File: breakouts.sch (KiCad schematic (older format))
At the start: 27 parts, among them P10 CONN_8, P11 CONN_5, P12 CONN_5, P13 CONN_6, P14 CONN_8, P15 CONN_5X2, P16 CONN_16, P17 CONN_16, P18 POWER, P19 PCM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

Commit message: A bunch of footprint arranging
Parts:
- P25: renamed from P?; footprint (none) -> replacement_kinesis_controller:Pin_Header_Staggered_Straight_1x02
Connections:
- net RST renamed RESET
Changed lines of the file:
@@
 PD1
 $Comp
-L GND #PWR35
+L GND #PWR034
 U 1 1 54E556E0
 P 2450 6050
-F 0 "#PWR35" H 2450 6050 30  0001 C CNN
+F 0 "#PWR034" H 2450 6050 30  0001 C CNN
 F 1 "GND" H 2450 5980 30  0001 C CNN
 F 2 "" H 2450 6050 60  0000 C CNN
@@
 $EndComp
 $Comp
-L GND #PWR37
+L GND #PWR035
 U 1 1 54E556E6
 P 4750 6050
-F 0 "#PWR37" H 4750 6050 30  0001 C CNN
+F 0 "#PWR035" H 4750 6050 30  0001 C CNN
 F 1 "GND" H 4750 5980 30  0001 C CNN
 F 2 "" H 4750 6050 60  0000 C CNN
@@
 $EndComp
 $Comp
-L VCC #PWR34
+L VCC #PWR036
 U 1 1 54E556EC
 P 2450 5800
-F 0 "#PWR34" H 2450 5900 30  0001 C CNN
+F 0 "#PWR036" H 2450 5900 30  0001 C CNN
 F 1 "VCC" H 2450 5900 30  0000 C CNN
 F 2 "" H 2450 5800 60  0000 C CNN
@@
 $EndComp
 $Comp
-L VCC #PWR36
+L VCC #PWR037
 U 1 1 54E556F2
 P 4750 5800
-F 0 "#PWR36" H 4750 5900 30  0001 C CNN
+F 0 "#PWR037" H 4750 5900 30  0001 C CNN
 F 1 "VCC" H 4750 5900 30  0000 C CNN
 F 2 "" H 4750 5800 60  0000 C CNN
@@
 	4750 5900 4750 5800
 $Comp
-L +5V #PWR39
+L +5V #PWR038
 U 1 1 54E569F6
 P 6250 2900
-F 0 "#PWR39" H 6250 2990 20  0001 C CNN
+F 0 "#PWR038" H 6250 2990 20  0001 C CNN
 F 1 "+5V" H 6250 2990 30  0000 C CNN
 F 2 "" H 6250 2900 60  0000 C CNN
@@
 PB4
 $Comp
-L GND #PWR38
+L GND #PWR039
 U 1 1 54E56A09
 P 5700 4500
-F 0 "#PWR38" H 5700 4500 30  0001 C CNN
+F 0 "#PWR039" H 5700 4500 30  0001 C CNN
 F 1 "GND" H 5700 4430 30  0001 C CNN
 F 2 "" H 5700 4500 60  0000 C CNN
@@
 PE6
 $Comp
-L +3.3V #PWR40
+L +3.3V #PWR040
 U 1 1 54E56A23
 P 7450 2900
-F 0 "#PWR40" H 7450 2860 30  0001 C CNN
+F 0 "#PWR040" H 7450 2860 30  0001 C CNN
 F 1 "+3.3V" H 7450 3010 30  0000 C CNN
 F 2 "" H 7450 2900 60  0000 C CNN
@@
 $EndComp
 Text GLabel 6100 4500 0    60   Input ~ 0
-RST
+RESET
 Wire Wire Line
 	7450 4500 7800 4500
@@
 	7450 4400 8000 4400
 $Comp
-L GND #PWR42
+L GND #PWR041
 U 1 1 54E56FF9
 P 8000 4500
-F 0 "#PWR42" H 8000 4500 30  0001 C CNN
+F 0 "#PWR041" H 8000 4500 30  0001 C CNN
 F 1 "GND" H 8000 4430 30  0001 C CNN
 F 2 "" H 8000 4500 60  0000 C CNN
@@
 	8000 4400 8000 4500
 $Comp
-L VCC #PWR41
+L VCC #PWR042
 U 1 1 54E42A55
 P 7800 4500
-F 0 "#PWR41" H 7800 4600 30  0001 C CNN
+F 0 "#PWR042" H 7800 4600 30  0001 C CNN
 F 1 "VCC" H 7800 4600 30  0000 C CNN
 F 2 "" H 7800 4500 60  0000 C CNN
@@
 W_NCTS
 $Comp
-L VCC #PWR47
+L VCC #PWR043
 U 1 1 54E5EB0B
 P 10050 5050
-F 0 "#PWR47" H 10050 5150 30  0001 C CNN
+F 0 "#PWR043" H 10050 5150 30  0001 C CNN
 F 1 "VCC" H 10050 5150 30  0000 C CNN
 F 2 "" H 10050 5050 60  0000 C CNN
@@
 $EndComp
 $Comp
-L GND #PWR46
+L GND #PWR044
 U 1 1 54E5EB11
 P 10050 4950
-F 0 "#PWR46" H 10050 4950 30  0001 C CNN
+F 0 "#PWR044" H 10050 4950 30  0001 C CNN
 F 1 "GND" H 10050 4880 30  0001 C CNN
 F 2 "" H 10050 4950 60  0000 C CNN
@@
 W_RESET
 $Comp
-L VCC #PWR45
+L VCC #PWR045
 U 1 1 54E5EB4D
 P 10050 1650
-F 0 "#PWR45" H 10050 1750 30  0001 C CNN
+F 0 "#PWR045" H 10050 1750 30  0001 C CNN
 F 1 "VCC" H 10050 1750 30  0000 C CNN
 F 2 "" H 10050 1650 60  0000 C CNN
@@
 $EndComp
 $Comp
-L +5V #PWR44
+L +5V #PWR046
 U 1 1 54E5EB53
 P 10050 1550
-F 0 "#PWR44" H 10050 1640 20  0001 C CNN
+F 0 "#PWR046" H 10050 1640 20  0001 C CNN
 F 1 "+5V" H 10050 1640 30  0000 C CNN
 F 2 "" H 10050 1550 60  0000 C CNN
@@
 $EndComp
 $Comp
-L GND #PWR43
+L GND #PWR047
 U 1 1 54E5EB59
 P 10050 1450
-F 0 "#PWR43" H 10050 1450 30  0001 C CNN
+F 0 "#PWR047" H 10050 1450 30  0001 C CNN
 F 1 "GND" H 10050 1380 30  0001 C CNN
 F 2 "" H 10050 1450 60  0000 C CNN
@@
 5V and VCC here are from the\nWT12 breakout board's built in\nregulator. Will this cause problems?
 $Comp
-L CONN_2 P?
+L CONN_2 P25
 U 1 1 54EA265F
 P 10600 5600
-F 0 "P?" V 10550 5600 40  0000 C CNN
+F 0 "P25" V 10550 5600 40  0000 C CNN
 F 1 "USB" V 10650 5600 40  0000 C CNN
-F 2 "" H 10600 5600 60  0000 C CNN
+F 2 "replacement_kinesis_controller:Pin_Header_Staggered_Straight_1x02" H 10600 5600 60  0001 C CNN
 F 3 "" H 10600 5600 60  0000 C CNN
 	1    10600 5600

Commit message: Ran a bunch of tracks for the 32u4
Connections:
- net RESET: now also P17.1 (P1); no longer P16.16 (P16)
- net VCC: now also P16.16 (P16); no longer P17.1 (P1)
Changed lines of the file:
@@
 	1    0    0    -1
 $EndComp
-Text GLabel 6100 4500 0    60   Input ~ 0
+Text GLabel 7600 4500 2    60   Input ~ 0
 RESET
-Wire Wire Line
-	7450 4500 7800 4500
-Wire Wire Line
-	6250 4500 6100 4500
 Wire Wire Line
 	6250 4400 5700 4400
@@
 L VCC #PWR042
 U 1 1 54E42A55
-P 7800 4500
-F 0 "#PWR042" H 7800 4600 30  0001 C CNN
-F 1 "VCC" H 7800 4600 30  0000 C CNN
-F 2 "" H 7800 4500 60  0000 C CNN
-F 3 "" H 7800 4500 60  0000 C CNN
-	1    7800 4500
+P 6000 4500
+F 0 "#PWR042" H 6000 4600 30  0001 C CNN
+F 1 "VCC" H 6000 4600 30  0000 C CNN
+F 2 "" H 6000 4500 60  0000 C CNN
+F 3 "" H 6000 4500 60  0000 C CNN
+	1    6000 4500
 	1    0    0    -1
 $EndComp
@@
 Wire Wire Line
 	10050 5700 10250 5700
+Wire Wire Line
+	7450 4500 7600 4500
+Wire Wire Line
+	6000 4500 6250 4500
 $EndSCHEMATC

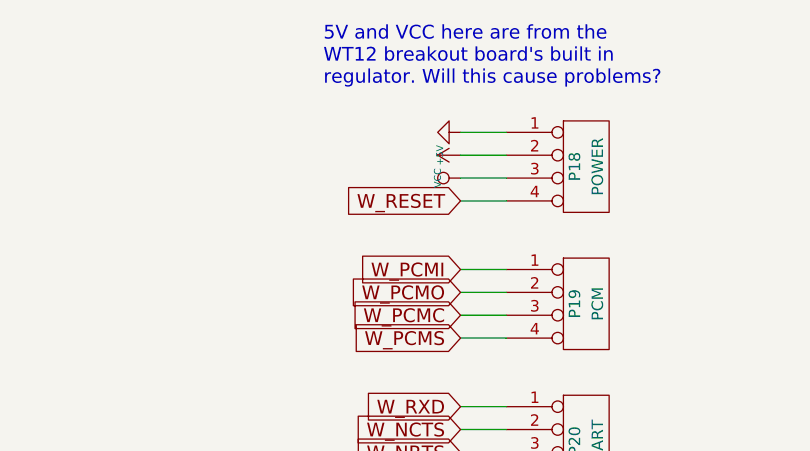
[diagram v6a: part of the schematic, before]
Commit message: Fix bluetooth breakout pin nets and add ground pour to USB boards
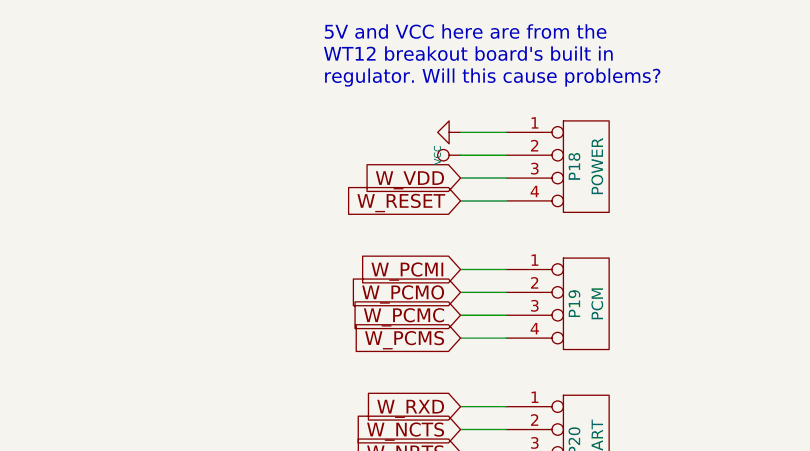
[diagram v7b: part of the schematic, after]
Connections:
- net +5V: no longer P18.2 (P2)
- net VCC: now also P18.2 (P2); no longer P18.3 (P3)
- new net W_VDD: P18.3 (P3)
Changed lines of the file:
@@
 L VCC #PWR045
 U 1 1 54E5EB4D
-P 10050 1650
-F 0 "#PWR045" H 10050 1750 30  0001 C CNN
-F 1 "VCC" H 10050 1750 30  0000 C CNN
-F 2 "" H 10050 1650 60  0000 C CNN
-F 3 "" H 10050 1650 60  0000 C CNN
-	1    10050 1650
-	0    -1   -1   0
-$EndComp
-$Comp
-L +5V #PWR046
-U 1 1 54E5EB53
 P 10050 1550
-F 0 "#PWR046" H 10050 1640 20  0001 C CNN
-F 1 "+5V" H 10050 1640 30  0000 C CNN
+F 0 "#PWR045" H 10050 1650 30  0001 C CNN
+F 1 "VCC" H 10050 1650 30  0000 C CNN
 F 2 "" H 10050 1550 60  0000 C CNN
 F 3 "" H 10050 1550 60  0000 C CNN
@@
 $EndComp
 $Comp
-L GND #PWR047
+L GND #PWR046
 U 1 1 54E5EB59
 P 10050 1450
-F 0 "#PWR047" H 10050 1450 30  0001 C CNN
+F 0 "#PWR046" H 10050 1450 30  0001 C CNN
 F 1 "GND" H 10050 1380 30  0001 C CNN
 F 2 "" H 10050 1450 60  0000 C CNN
@@
 Wire Wire Line
 	6000 4500 6250 4500
+Text GLabel 10050 1650 0    60   Input ~ 0
+W_VDD
 $EndSCHEMATC

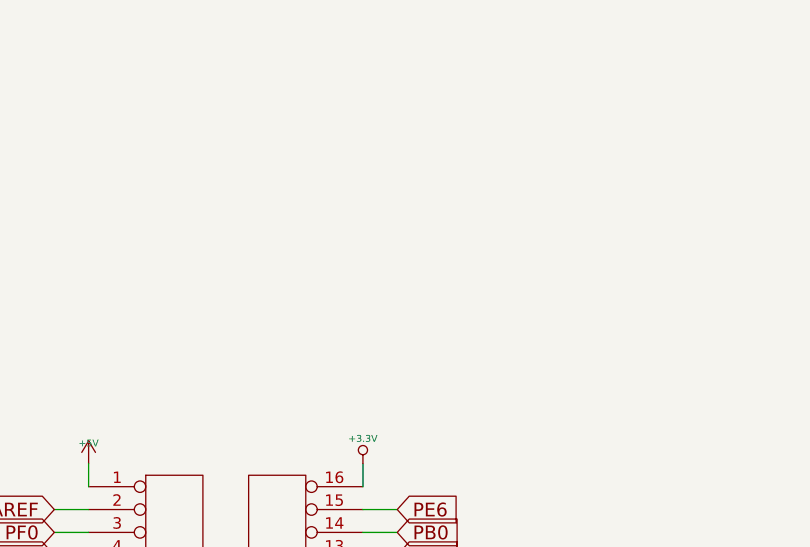
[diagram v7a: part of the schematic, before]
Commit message: Add breakout for LED chain output
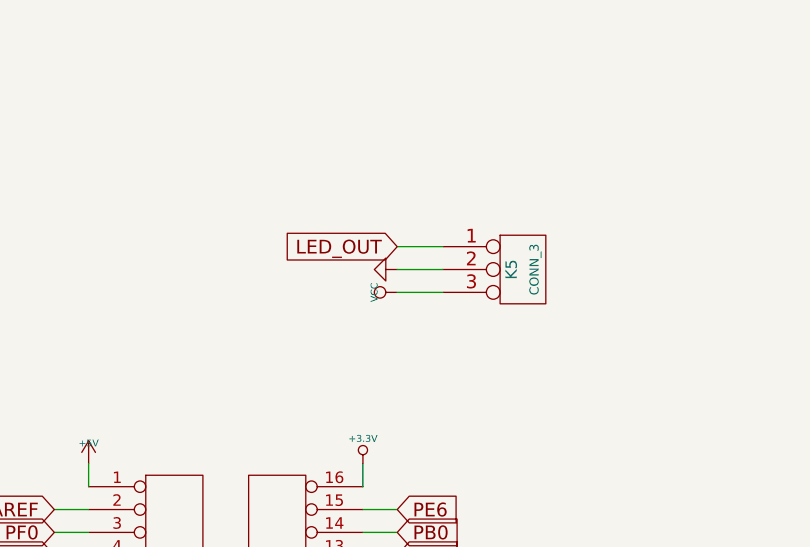
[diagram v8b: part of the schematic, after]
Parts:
- added K5: CONN_3, replacement_kinesis_controller:Pin_Header_Staggered_Straight_1x03, symbol CONN_3
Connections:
- net GND: now also K5.2 (PM)
- net VCC: now also K5.3 (P3)
- new net LED_OUT: K5.1 (P1)
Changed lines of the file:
@@
 PD1
 $Comp
-L GND #PWR034
+L GND #PWR35
 U 1 1 54E556E0
 P 2450 6050
-F 0 "#PWR034" H 2450 6050 30  0001 C CNN
+F 0 "#PWR35" H 2450 6050 30  0001 C CNN
 F 1 "GND" H 2450 5980 30  0001 C CNN
 F 2 "" H 2450 6050 60  0000 C CNN
@@
 $EndComp
 $Comp
-L GND #PWR035
+L GND #PWR37
 U 1 1 54E556E6
 P 4750 6050
-F 0 "#PWR035" H 4750 6050 30  0001 C CNN
+F 0 "#PWR37" H 4750 6050 30  0001 C CNN
 F 1 "GND" H 4750 5980 30  0001 C CNN
 F 2 "" H 4750 6050 60  0000 C CNN
@@
 $EndComp
 $Comp
-L VCC #PWR036
+L VCC #PWR34
 U 1 1 54E556EC
 P 2450 5800
-F 0 "#PWR036" H 2450 5900 30  0001 C CNN
+F 0 "#PWR34" H 2450 5900 30  0001 C CNN
 F 1 "VCC" H 2450 5900 30  0000 C CNN
 F 2 "" H 2450 5800 60  0000 C CNN
@@
 $EndComp
 $Comp
-L VCC #PWR037
+L VCC #PWR36
 U 1 1 54E556F2
 P 4750 5800
-F 0 "#PWR037" H 4750 5900 30  0001 C CNN
+F 0 "#PWR36" H 4750 5900 30  0001 C CNN
 F 1 "VCC" H 4750 5900 30  0000 C CNN
 F 2 "" H 4750 5800 60  0000 C CNN
@@
 	4750 5900 4750 5800
 $Comp
-L +5V #PWR038
+L +5V #PWR40
 U 1 1 54E569F6
 P 6250 2900
-F 0 "#PWR038" H 6250 2990 20  0001 C CNN
+F 0 "#PWR40" H 6250 2990 20  0001 C CNN
 F 1 "+5V" H 6250 2990 30  0000 C CNN
 F 2 "" H 6250 2900 60  0000 C CNN
@@
 PB4
 $Comp
-L GND #PWR039
+L GND #PWR38
 U 1 1 54E56A09
 P 5700 4500
-F 0 "#PWR039" H 5700 4500 30  0001 C CNN
+F 0 "#PWR38" H 5700 4500 30  0001 C CNN
 F 1 "GND" H 5700 4430 30  0001 C CNN
 F 2 "" H 5700 4500 60  0000 C CNN
@@
 PE6
 $Comp
-L +3.3V #PWR040
+L +3.3V #PWR41
 U 1 1 54E56A23
 P 7450 2900
-F 0 "#PWR040" H 7450 2860 30  0001 C CNN
+F 0 "#PWR41" H 7450 2860 30  0001 C CNN
 F 1 "+3.3V" H 7450 3010 30  0000 C CNN
 F 2 "" H 7450 2900 60  0000 C CNN
@@
 	7450 4400 8000 4400
 $Comp
-L GND #PWR041
+L GND #PWR44
 U 1 1 54E56FF9
 P 8000 4500
-F 0 "#PWR041" H 8000 4500 30  0001 C CNN
+F 0 "#PWR44" H 8000 4500 30  0001 C CNN
 F 1 "GND" H 8000 4430 30  0001 C CNN
 F 2 "" H 8000 4500 60  0000 C CNN
@@
 	8000 4400 8000 4500
 $Comp
-L VCC #PWR042
+L VCC #PWR39
 U 1 1 54E42A55
 P 6000 4500
-F 0 "#PWR042" H 6000 4600 30  0001 C CNN
+F 0 "#PWR39" H 6000 4600 30  0001 C CNN
 F 1 "VCC" H 6000 4600 30  0000 C CNN
 F 2 "" H 6000 4500 60  0000 C CNN
@@
 W_NCTS
 $Comp
-L VCC #PWR043
+L VCC #PWR48
 U 1 1 54E5EB0B
 P 10050 5050
-F 0 "#PWR043" H 10050 5150 30  0001 C CNN
+F 0 "#PWR48" H 10050 5150 30  0001 C CNN
 F 1 "VCC" H 10050 5150 30  0000 C CNN
 F 2 "" H 10050 5050 60  0000 C CNN
@@
 $EndComp
 $Comp
-L GND #PWR044
+L GND #PWR47
 U 1 1 54E5EB11
 P 10050 4950
-F 0 "#PWR044" H 10050 4950 30  0001 C CNN
+F 0 "#PWR47" H 10050 4950 30  0001 C CNN
 F 1 "GND" H 10050 4880 30  0001 C CNN
 F 2 "" H 10050 4950 60  0000 C CNN
@@
 W_RESET
 $Comp
-L VCC #PWR045
+L VCC #PWR46
 U 1 1 54E5EB4D
 P 10050 1550
-F 0 "#PWR045" H 10050 1650 30  0001 C CNN
+F 0 "#PWR46" H 10050 1650 30  0001 C CNN
 F 1 "VCC" H 10050 1650 30  0000 C CNN
 F 2 "" H 10050 1550 60  0000 C CNN
@@
 $EndComp
 $Comp
-L GND #PWR046
+L GND #PWR45
 U 1 1 54E5EB59
 P 10050 1450
-F 0 "#PWR046" H 10050 1450 30  0001 C CNN
+F 0 "#PWR45" H 10050 1450 30  0001 C CNN
 F 1 "GND" H 10050 1380 30  0001 C CNN
 F 2 "" H 10050 1450 60  0000 C CNN
@@
 Text GLabel 10050 1650 0    60   Input ~ 0
 W_VDD
+$Comp
+L CONN_3 K5
+U 1 1 55047ED4
+P 8150 2050
+F 0 "K5" V 8100 2050 50  0000 C CNN
+F 1 "CONN_3" V 8200 2050 40  0000 C CNN
+F 2 "replacement_kinesis_controller:Pin_Header_Staggered_Straight_1x03" H 8150 2050 60  0001 C CNN
+F 3 "" H 8150 2050 60  0000 C CNN
+	1    8150 2050
+	1    0    0    -1
+$EndComp
+Text GLabel 7600 1950 0    60   Input ~ 0
+LED_OUT
+$Comp
+L GND #PWR42
+U 1 1 55048034
+P 7600 2050
+F 0 "#PWR42" H 7600 2050 30  0001 C CNN
+F 1 "GND" H 7600 1980 30  0001 C CNN
+F 2 "" H 7600 2050 60  0000 C CNN
+F 3 "" H 7600 2050 60  0000 C CNN
+	1    7600 2050
+	0    1    1    0
+$EndComp
+$Comp
+L VCC #PWR43
+U 1 1 55048077
+P 7600 2150
+F 0 "#PWR43" H 7600 2250 30  0001 C CNN
+F 1 "VCC" H 7600 2250 30  0000 C CNN
+F 2 "" H 7600 2150 60  0000 C CNN
+F 3 "" H 7600 2150 60  0000 C CNN
+	1    7600 2150
+	0    -1   -1   0
+$EndComp
+Wire Wire Line
+	7600 1950 7800 1950
+Wire Wire Line
+	7600 2050 7800 2050
+Wire Wire Line
+	7600 2150 7800 2150
 $EndSCHEMATC
